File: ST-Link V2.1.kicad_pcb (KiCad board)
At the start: 2 copper layers, 31.8 x 20.9 mm, 43 parts, among them J2 Conn_01x06, J3 Conn_01x08, J4 Conn_01x08, Q1 MMBT3904, U1 USBLC6-2SC6, U2 stm32, U3 MIC5219-3.3, X1 8MHz

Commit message: added 1C1R
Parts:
- removed USB: USB_OTG, Connectors_USB:USB_Micro-B_Molex-105017-0001
- added C7: 1uF, Capacitors_SMD:C_0603, B.Cu at (143.5, 103.0)
- added J1: USB_OTG, Connectors_USB:USB_Micro-B_Molex-105017-0001, F.Cu at (121.2, 108.6)
- added R15: 10K, Resistors_SMD:R_0603, B.Cu at (141.9, 103.0)
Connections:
- U2 pad 0: (no net) -> GND
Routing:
- net GND: track 110.1 -> 136.1 mm
- net /T_NRST: track 18.2 -> 23.2 mm
- net /3V3_ST_LINK: track 117.8 -> 120.0 mm, vias 11 -> 12
- net /LED_STLINK: track 24.8 -> 23.4 mm
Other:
- net class Default: via_dia 0.45 -> 0.453
- net class new: via_dia 0.45 -> 0.453

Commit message: commit for deletion unused vias n tracks
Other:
- board text added: "___ RST"
- board text removed: "nRST"
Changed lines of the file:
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@@
     (links 120)
     (no_connects 0)
-    (area 118.624999 98.124999 150.575001 119.175001)
+    (area 116.745201 95.429981 153.401619 119.695099)
     (thickness 1.6)
     (drawings 20)
@@
   )
   (setup
-    (last_trace_width 0.4)
+    (last_trace_width 0.25)
     (user_trace_width 0.4)
     (user_trace_width 0.6)
@@
     (effects (font (size 1 1) (thickness 0.153)) (justify mirror))
   )
-  (gr_text JTMS (at 144.95 104.85) (layer B.SilkS)
+  (gr_text JTMS (at 144.975 105.275) (layer B.SilkS)
     (effects (font (size 1 1) (thickness 0.153)) (justify mirror))
   )
-  (gr_text nRST (at 144.875 102.675) (layer B.SilkS)
+  (gr_text "___\nRST" (at 145.375 102.375) (layer B.SilkS)
     (effects (font (size 1 1) (thickness 0.153)) (justify mirror))
   )

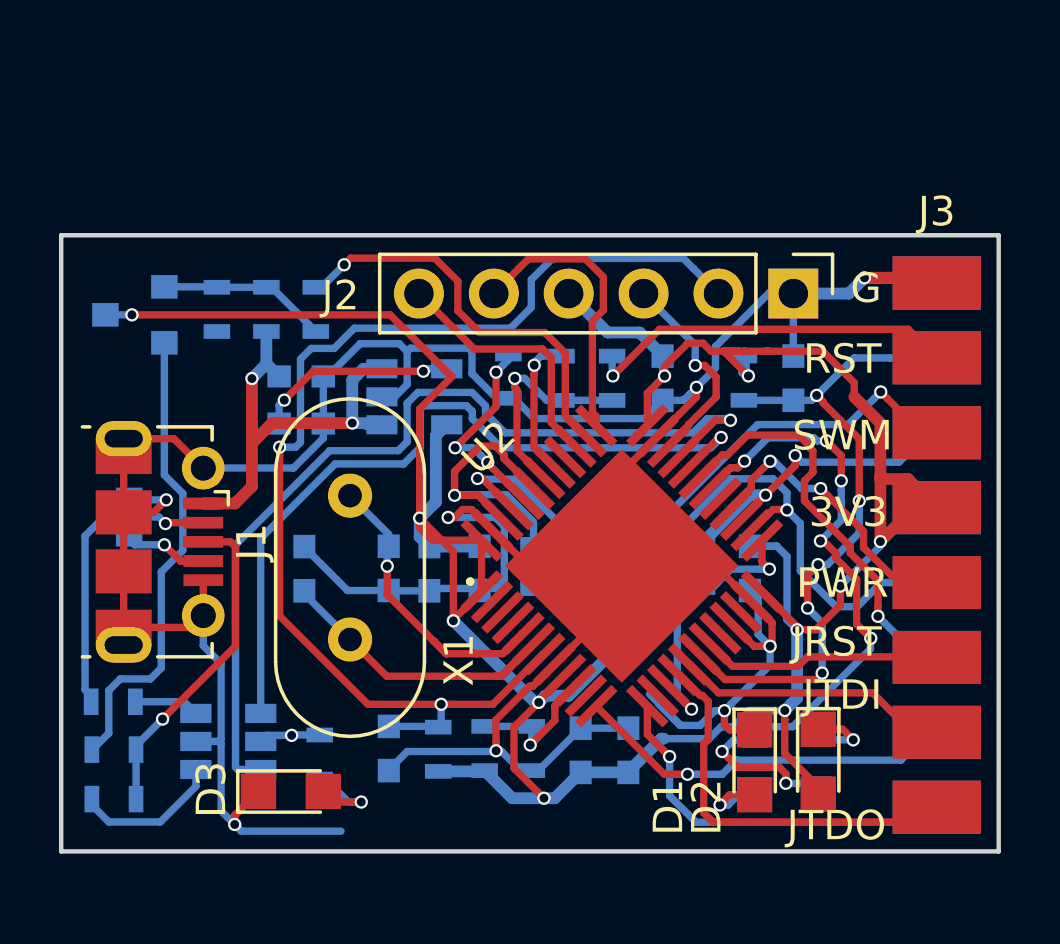
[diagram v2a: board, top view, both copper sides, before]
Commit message: changed the Stm layout
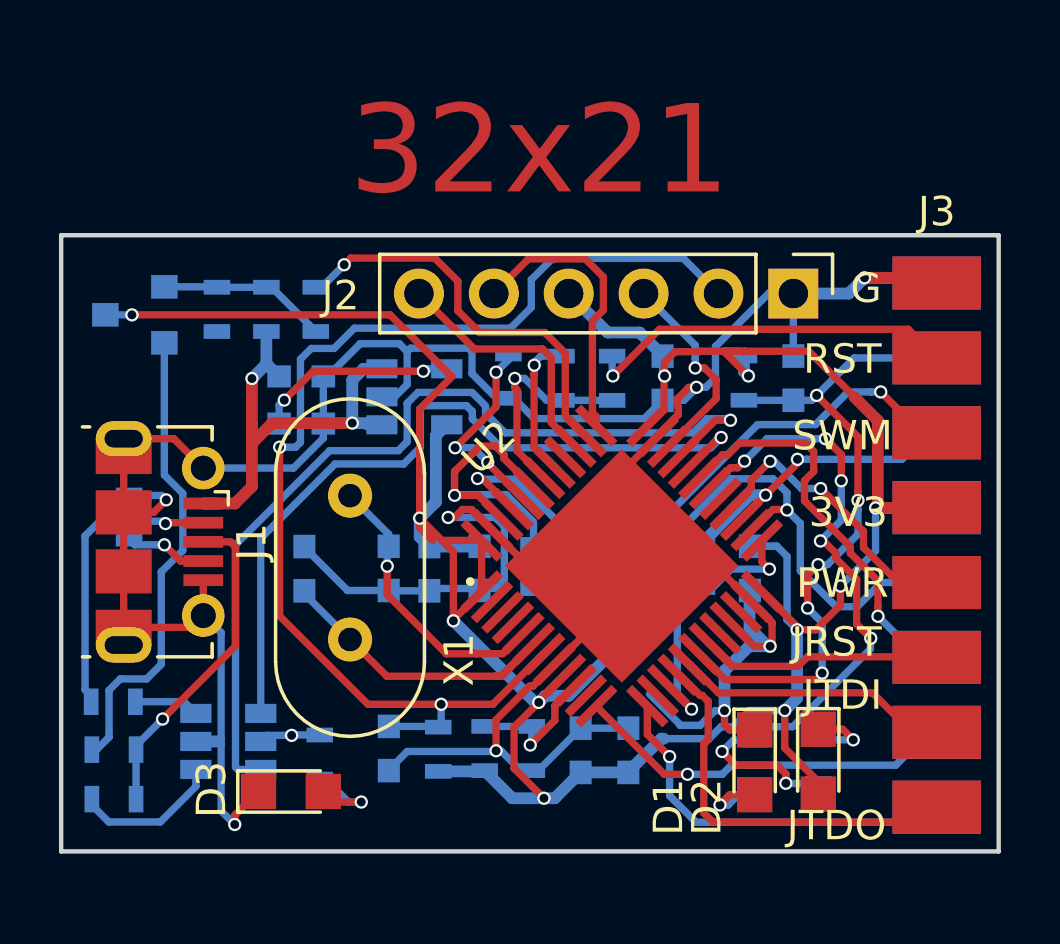
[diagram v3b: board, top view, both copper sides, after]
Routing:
- net /3V3_ST_LINK: track 120.0 -> 110.8 mm
- net GND: track 136.1 -> 132.4 mm
- net Net-(C3-Pad2): track 10.3 -> 9.71 mm
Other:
- board text added: "32x21"

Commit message: checked schematic
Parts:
- removed C7: 1uF, Capacitors_SMD:C_0603
- removed R15: 10K, Resistors_SMD:R_0603
- added R22: 100K, Resistors_SMD:R_0603, B.Cu at (138.7, 112.7)
- added R23: 10K, Resistors_SMD:R_0603, B.Cu at (141.0, 112.6)
- added R24: 10K, Resistors_SMD:R_0603, B.Cu at (133.1, 112.8)
- D1: value LED -> RED_LED
- D2: value LED -> BLUE_LED
- U2: footprint UFQFPN48:UFQFPN48 -> QFPN48:UFQFPN48
- moved C6 0.06 mm to (142.1, 109.4)
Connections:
- U2 pad 21: GND -> Net-(R23-Pad2)
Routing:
- net Net-(R22-Pad2): track 0.00 -> 11.1 mm, vias 0 -> 1
- net /3V3_ST_LINK: track 110.8 -> 103.4 mm, vias 12 -> 11
- net GND: track 132.4 -> 138.8 mm, vias 8 -> 10
- net Net-(R23-Pad2): track 0.00 -> 5.12 mm, vias 0 -> 1
- net /STLINK_TX: track 13.1 -> 16.4 mm
- net Net-(R24-Pad1): track 0.00 -> 2.99 mm, vias 0 -> 1
- net /T_SWDIO_IN: track 3.89 -> 5.75 mm
- net /LED_STLINK: track 23.4 -> 24.8 mm
- net /T_SWCLK_JTCK: track 21.8 -> 23.1 mm
- net /STLINK_RX: track 13.1 -> 13.7 mm
- net /T_NRST: track 23.1 -> 23.7 mm

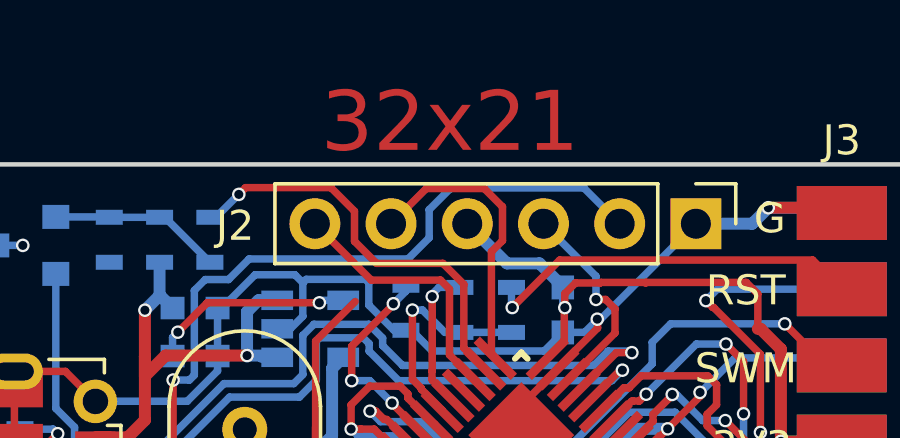
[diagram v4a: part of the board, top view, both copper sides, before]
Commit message: need to change the footprint of the led
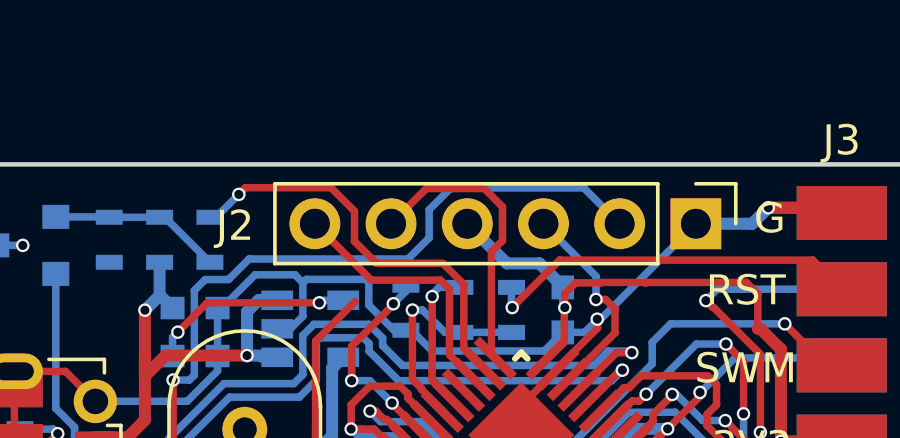
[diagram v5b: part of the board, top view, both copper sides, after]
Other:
- board text removed: "32x21"
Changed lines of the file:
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@@
     (links 124)
     (no_connects 0)
-    (area 116.745201 92.85 153.401619 119.875197)
+    (area 116.745201 95.14 153.401619 119.875197)
     (thickness 1.6)
-    (drawings 21)
+    (drawings 22)
     (tracks 768)
     (zones 0)
@@
     (31 B.Cu signal)
     (32 B.Adhes user hide)
-    (33 F.Adhes user hide)
+    (33 F.Adhes user)
     (34 B.Paste user)
     (35 F.Paste user)
@@
     )
   )
-  (gr_text 32x21 (at 135.34 96.79) (layer F.Cu)
-    (effects (font (size 2 2) (thickness 0.5)))
+  (dimension 20.900002 (width 0.3) (layer F.Adhes)
+    (gr_text "20.900 mm" (at 116.545015 108.648966 89.97258575) (layer F.Adhes)
+      (effects (font (size 1.5 1.5) (thickness 0.3)))
+    )
+    (feature1 (pts (xy 118.7 119.1) (xy 115.190015 119.09832)))
+    (feature2 (pts (xy 118.71 98.2) (xy 115.200015 98.19832)))
+    (crossbar (pts (xy 117.900015 98.199612) (xy 117.890015 119.099612)))
+    (arrow1a (pts (xy 117.890015 119.099612) (xy 117.304133 117.972828)))
+    (arrow1b (pts (xy 117.890015 119.099612) (xy 118.476975 117.973389)))
+    (arrow2a (pts (xy 117.900015 98.199612) (xy 117.313055 99.325835)))
+    (arrow2b (pts (xy 117.900015 98.199612) (xy 118.485897 99.326396)))
+  )
+  (dimension 31.8 (width 0.3) (layer F.Adhes)
+    (gr_text "31.800 mm" (at 134.6 96.04) (layer F.Adhes)
+      (effects (font (size 1.5 1.5) (thickness 0.3)))
+    )
+    (feature1 (pts (xy 150.5 98.2) (xy 150.5 94.69)))
+    (feature2 (pts (xy 118.7 98.2) (xy 118.7 94.69)))
+    (crossbar (pts (xy 118.7 97.39) (xy 150.5 97.39)))
+    (arrow1a (pts (xy 150.5 97.39) (xy 149.373496 97.976421)))
+    (arrow1b (pts (xy 150.5 97.39) (xy 149.373496 96.803579)))
+    (arrow2a (pts (xy 118.7 97.39) (xy 119.826504 97.976421)))
+    (arrow2b (pts (xy 118.7 97.39) (xy 119.826504 96.803579)))
   )
   (gr_text RX (at 145.8 118.2) (layer B.SilkS)

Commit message: added BOM,updated size and gerber file
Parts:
- D1, D2, D3: footprint LEDs:LED_0805 -> MetalPad:LED_0805
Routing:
- net GND: track 138.8 -> 131.6 mm, vias 10 -> 9
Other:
- board size 31.8 x 20.9 mm -> 31.8 x 23 mm

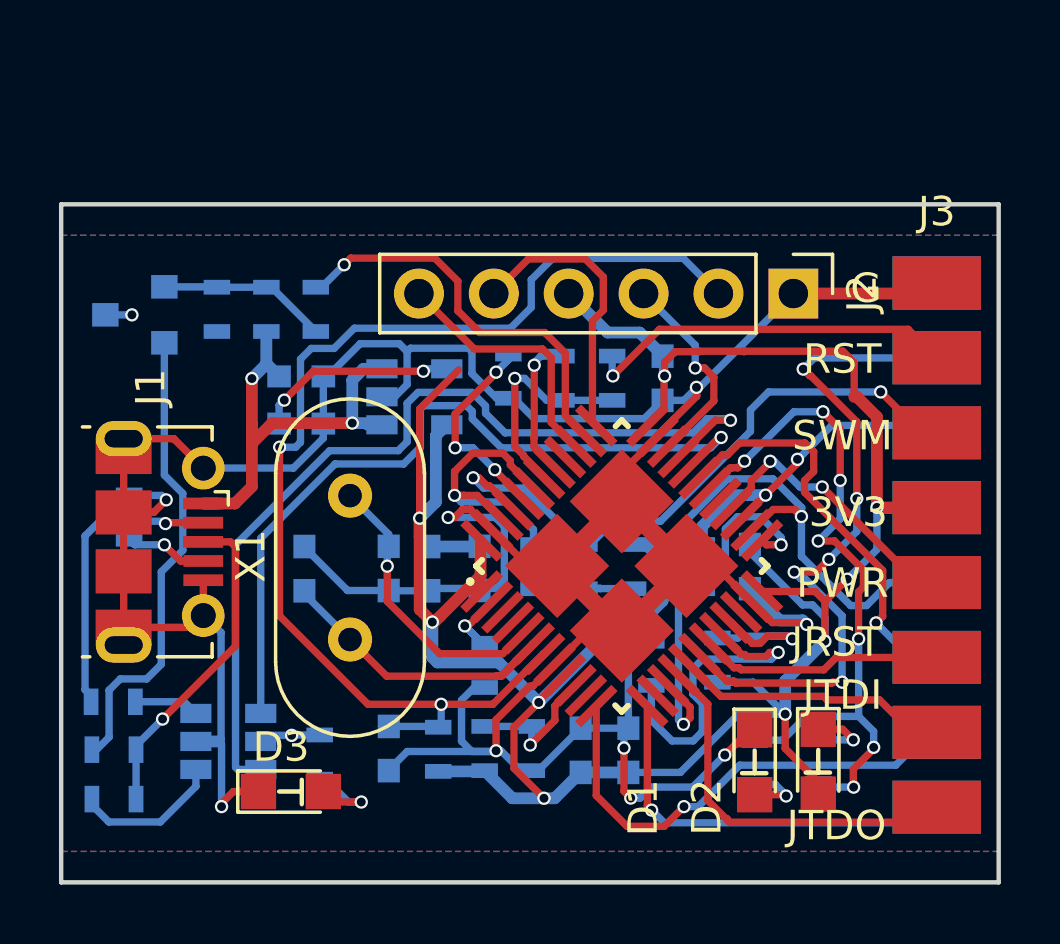
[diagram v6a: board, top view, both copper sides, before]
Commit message: changed the size to eco user and adjusted the size of text
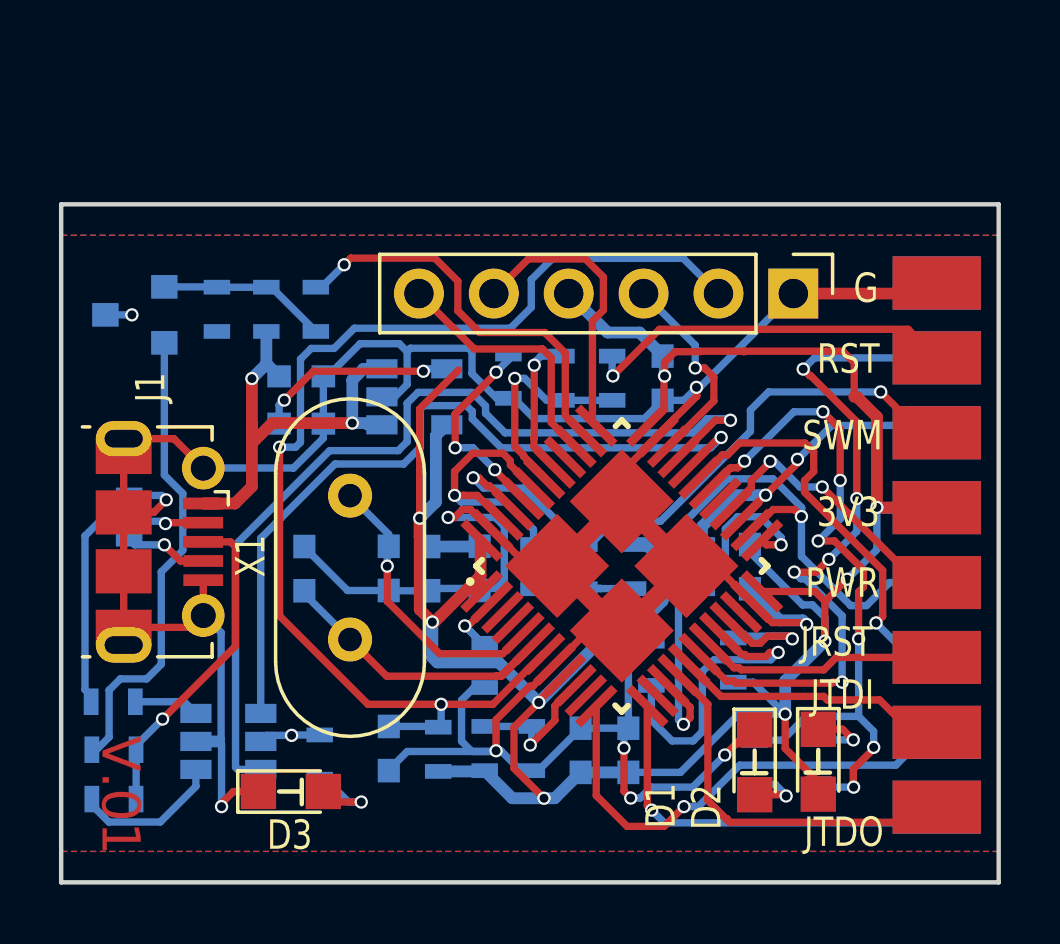
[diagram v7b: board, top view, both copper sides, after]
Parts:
- moved R23 0.54 mm to (141.5, 112.6)
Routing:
- net Net-(R23-Pad2): track 5.12 -> 4.42 mm
- net /3V3_ST_LINK: track 103.4 -> 102.8 mm
- net Net-(R22-Pad2): track 11.1 -> 10.6 mm
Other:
- board text added: "V.01"

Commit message: changed the footprint of the U2
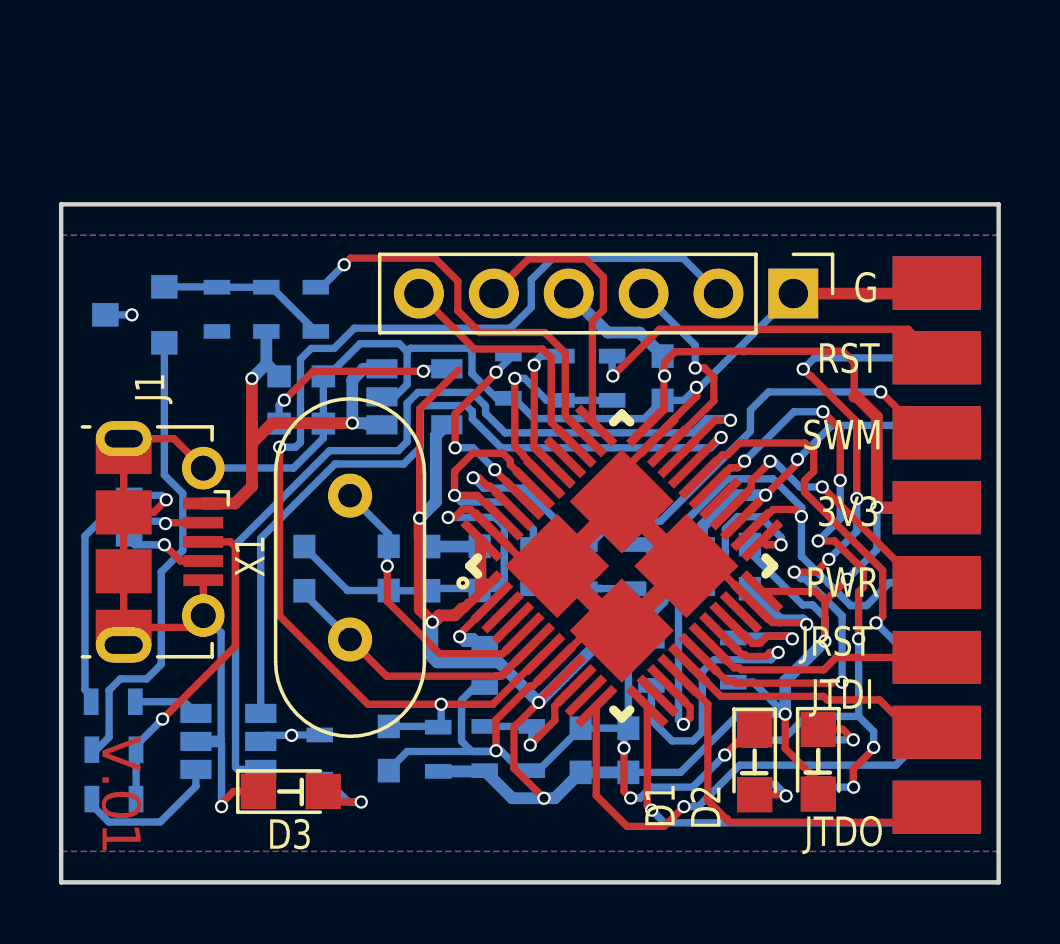
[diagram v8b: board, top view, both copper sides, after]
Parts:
- U2: footprint QFPN48:UFQFPN48 -> QFPN48:QFN_QFP48
